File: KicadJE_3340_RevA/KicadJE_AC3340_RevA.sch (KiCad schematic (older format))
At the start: 132 parts

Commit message: Annotate
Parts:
- gave numbers to parts that had none: 125

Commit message: Update KicadJE_AC3340_RevA.sch
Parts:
- removed D119: LED, LED_SMD:LED_0805_2012Metric_Pad1.15x1.40mm_HandSolder, symbol Device:LED
- added R?: OPEN, Resistor_SMD:R_0805_2012Metric_Pad1.15x1.40mm_HandSolder, symbol Device:R
- R156: value 1k -> 100k
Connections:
- net 3CVIn1: now also R156.1
- net 3Octave: now also R151.2, U103.3 (+)
- net GND: now also R?.2
- net at R150.2, R153.2, U103.7: no longer R151.2, U103.3 (+)
- net at R152.2, U103.2 (-): now also R?.1
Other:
- moved on the sheet: R151, R152, R156, U103A
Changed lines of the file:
@@
 L Amplifier_Operational:TL072 U?
 U 1 1 614891B3
-P 7725 4275
+P 9750 6075
 AR Path="/5D99B81E/614891B3" Ref="U?"  Part="3"
 AR Path="/5D99B7BA/614891B3" Ref="U?"  Part="1"
@@
 AR Path="/5F49A670/614891B3" Ref="U?"  Part="1"
 AR Path="/614891B3" Ref="U103"  Part="1"
-F 0 "U103" H 7625 4300 50  0000 C CNN
-F 1 "TL072" H 7650 4225 50  0000 C CNN
-F 2 "AJ-Dropbox-Kicad:AJ_SO-8_5.3x6.2mm_P1.27mm" H 7725 4275 50  0001 C CNN
-F 3 "http://www.ti.com/lit/ds/symlink/tl071.pdf" H 7725 4275 50  0001 C CNN
-	1    7725 4275
+F 0 "U103" H 9650 6100 50  0000 C CNN
+F 1 "TL072" H 9675 6025 50  0000 C CNN
+F 2 "AJ-Dropbox-Kicad:AJ_SO-8_5.3x6.2mm_P1.27mm" H 9750 6075 50  0001 C CNN
+F 3 "http://www.ti.com/lit/ds/symlink/tl071.pdf" H 9750 6075 50  0001 C CNN
+	1    9750 6075
 	1    0    0    -1
 $EndComp
 Wire Wire Line
-	7425 4375 7400 4375
+	9450 6175 9425 6175
 Wire Wire Line
-	7400 4375 7400 4525
+	9425 6175 9425 6325
 Wire Wire Line
-	7400 4525 7575 4525
+	9425 6325 9600 6325
 Wire Wire Line
-	8050 4525 8050 4275
+	10075 6325 10075 6075
 Wire Wire Line
-	8050 4275 8025 4275
+	10075 6075 10050 6075
 $Comp
 L Device:R R156
 U 1 1 614891BF
-P 8200 4275
+P 10225 6075
 AR Path="/614891BF" Ref="R156"  Part="1"
 AR Path="/5C8C5FC0/614891BF" Ref="R?"  Part="1"
@@
 AR Path="/5E62ACA1/614891BF" Ref="R?"  Part="1"
 AR Path="/5F49A670/614891BF" Ref="R?"  Part="1"
-F 0 "R156" V 8100 4200 50  0000 C CNN
-F 1 "1k" V 8200 4275 50  0000 C CNN
-F 2 "Resistor_SMD:R_0805_2012Metric_Pad1.15x1.40mm_HandSolder" V 8130 4275 50  0001 C CNN
-F 3 "~" H 8200 4275 50  0001 C CNN
-	1    8200 4275
+F 0 "R156" V 10125 6000 50  0000 C CNN
+F 1 "100k" V 10225 6075 50  0000 C CNN
+F 2 "Resistor_SMD:R_0805_2012Metric_Pad1.15x1.40mm_HandSolder" V 10155 6075 50  0001 C CNN
+F 3 "~" H 10225 6075 50  0001 C CNN
+	1    10225 6075
 	0    1    1    0
 $EndComp
-Connection ~ 8050 4275
+Connection ~ 10075 6075
 Wire Wire Line
 	2400 1125 2325 1125
@@
 L Device:R R151
 U 1 1 61551447
-P 7725 3950
+P 9750 5750
 AR Path="/61551447" Ref="R151"  Part="1"
 AR Path="/5C8C5FC0/61551447" Ref="R?"  Part="1"
@@
 AR Path="/5E62ACA1/61551447" Ref="R?"  Part="1"
 AR Path="/5F49A670/61551447" Ref="R?"  Part="1"
-F 0 "R151" V 7625 3875 50  0000 C CNN
-F 1 "OPEN" V 7725 3950 50  0000 C CNN
-F 2 "Resistor_SMD:R_0805_2012Metric_Pad1.15x1.40mm_HandSolder" V 7655 3950 50  0001 C CNN
-F 3 "~" H 7725 3950 50  0001 C CNN
-	1    7725 3950
+F 0 "R151" V 9650 5675 50  0000 C CNN
+F 1 "OPEN" V 9750 5750 50  0000 C CNN
+F 2 "Resistor_SMD:R_0805_2012Metric_Pad1.15x1.40mm_HandSolder" V 9680 5750 50  0001 C CNN
+F 3 "~" H 9750 5750 50  0001 C CNN
+	1    9750 5750
 	0    1    1    0
 $EndComp
 Wire Wire Line
-	7400 4175 7400 3950
+	9425 5975 9425 5750
 Wire Wire Line
-	7400 3950 7575 3950
+	9425 5750 9600 5750
 Wire Wire Line
-	7400 4175 7425 4175
+	9425 5975 9450 5975
 Wire Wire Line
-	8050 4275 8050 3950
+	10075 6075 10075 5750
 Wire Wire Line
-	8050 3950 7875 3950
+	10075 5750 9900 5750
 $Comp
 L Envelope-cache-2018-08-04-13-00-04:GND #PWR0125
@@
 Wire Wire Line
 	7550 3750 7400 3750
-Wire Wire Line
-	7400 3750 7400 3950
-Connection ~ 7400 3950
 $Comp
 L Device:R R152
 U 1 1 616AB5FE
-P 7725 4525
+P 9750 6325
 AR Path="/616AB5FE" Ref="R152"  Part="1"
 AR Path="/5C8C5FC0/616AB5FE" Ref="R?"  Part="1"
@@
 AR Path="/5E62ACA1/616AB5FE" Ref="R?"  Part="1"
 AR Path="/5F49A670/616AB5FE" Ref="R?"  Part="1"
-F 0 "R152" V 7825 4450 50  0000 C CNN
-F 1 "0R" V 7725 4525 50  0000 C CNN
-F 2 "Resistor_SMD:R_0805_2012Metric_Pad1.15x1.40mm_HandSolder" V 7655 4525 50  0001 C CNN
-F 3 "~" H 7725 4525 50  0001 C CNN
-	1    7725 4525
+F 0 "R152" V 9850 6250 50  0000 C CNN
+F 1 "0R" V 9750 6325 50  0000 C CNN
+F 2 "Resistor_SMD:R_0805_2012Metric_Pad1.15x1.40mm_HandSolder" V 9680 6325 50  0001 C CNN
+F 3 "~" H 9750 6325 50  0001 C CNN
+	1    9750 6325
 	0    1    1    0
 $EndComp
 Wire Wire Line
-	7875 4525 8050 4525
+	9900 6325 10075 6325
+Text GLabel 10525 6075 2    50   Input ~ 0
+3CVIn1
+Wire Wire Line
+	10375 6075 10525 6075
+Text GLabel 9300 5975 0    50   Input ~ 0
+3Octave
+Wire Wire Line
+	9300 5975 9425 5975
+Connection ~ 9425 5975
 $Comp
-L Device:LED D?
-U 1 1 616ABD5F
-P 8375 4500
-AR Path="/5E4B0DD9/616ABD5F" Ref="D?"  Part="1"
-AR Path="/5E62ACA1/616ABD5F" Ref="D?"  Part="1"
-AR Path="/5F49A670/616ABD5F" Ref="D?"  Part="1"
-AR Path="/616ABD5F" Ref="D119"  Part="1"
-F 0 "D119" H 8525 4575 50  0000 R CNN
-F 1 "LED" H 8475 4650 50  0000 R CNN
-F 2 "LED_SMD:LED_0805_2012Metric_Pad1.15x1.40mm_HandSolder" H 8375 4500 50  0001 C CNN
-F 3 "~" H 8375 4500 50  0001 C CNN
-	1    8375 4500
-	0    -1   -1   0
+L Device:R R?
+U 1 1 5E78950E
+P 9200 6325
+AR Path="/5E78950E" Ref="R?"  Part="1"
+AR Path="/5C8C5FC0/5E78950E" Ref="R?"  Part="1"
+AR Path="/5CAAE8D3/5E78950E" Ref="R?"  Part="1"
+AR Path="/5E4B0DD9/5E78950E" Ref="R?"  Part="1"
+AR Path="/5E62ACA1/5E78950E" Ref="R?"  Part="1"
+AR Path="/5F49A670/5E78950E" Ref="R?"  Part="1"
+F 0 "R?" V 9100 6250 50  0000 C CNN
+F 1 "OPEN" V 9200 6325 50  0000 C CNN
+F 2 "Resistor_SMD:R_0805_2012Metric_Pad1.15x1.40mm_HandSolder" V 9130 6325 50  0001 C CNN
+F 3 "~" H 9200 6325 50  0001 C CNN
+	1    9200 6325
+	0    1    1    0
 $EndComp
 $Comp
-L Envelope-cache-2018-08-04-13-00-04:GND #PWR0142
-U 1 1 616AD7D0
-P 8375 4700
-AR Path="/616AD7D0" Ref="#PWR0142"  Part="1"
-AR Path="/5C8C5FC0/616AD7D0" Ref="#PWR?"  Part="1"
-AR Path="/5CAAE8D3/616AD7D0" Ref="#PWR?"  Part="1"
-AR Path="/5E4B0DD9/616AD7D0" Ref="#PWR?"  Part="1"
-AR Path="/5E62ACA1/616AD7D0" Ref="#PWR?"  Part="1"
-AR Path="/5F49A670/616AD7D0" Ref="#PWR?"  Part="1"
-F 0 "#PWR0142" H 8375 4450 50  0001 C CNN
-F 1 "GND" H 8380 4527 50  0000 C CNN
-F 2 "" H 8375 4700 50  0001 C CNN
-F 3 "" H 8375 4700 50  0001 C CNN
-	1    8375 4700
+L Envelope-cache-2018-08-04-13-00-04:GND #PWR?
+U 1 1 5E789A07
+P 8975 6325
+AR Path="/5E789A07" Ref="#PWR?"  Part="1"
+AR Path="/5C8C5FC0/5E789A07" Ref="#PWR?"  Part="1"
+AR Path="/5CAAE8D3/5E789A07" Ref="#PWR?"  Part="1"
+AR Path="/5E4B0DD9/5E789A07" Ref="#PWR?"  Part="1"
+AR Path="/5E62ACA1/5E789A07" Ref="#PWR?"  Part="1"
+AR Path="/5F49A670/5E789A07" Ref="#PWR?"  Part="1"
+F 0 "#PWR?" H 8975 6075 50  0001 C CNN
+F 1 "GND" H 8980 6152 50  0000 C CNN
+F 2 "" H 8975 6325 50  0001 C CNN
+F 3 "" H 8975 6325 50  0001 C CNN
+	1    8975 6325
 	1    0    0    -1
 $EndComp
 Wire Wire Line
-	8375 4700 8375 4650
+	8975 6325 9050 6325
 Wire Wire Line
-	8375 4275 8350 4275
-Wire Wire Line
-	8375 4350 8375 4275
+	9350 6325 9425 6325
+Connection ~ 9425 6325
 $EndSCHEMATC

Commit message: base PCB
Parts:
- gave numbers to parts that had none: 1
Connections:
- net +12L is gone; now on net +12VA: R117.2
- net +12V is gone; now on net +12VA: D101.1 (K), D103.1 (K), D105.1 (K), D106.1 (K), D109.1 (K), D111.1 (K), R129.1
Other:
- moved on the sheet: J111, R151, R152, R156, R163, U103A

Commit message: DRC Done
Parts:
- added C118, C119: 100n, Capacitor_SMD:C_0805_2012Metric_Pad1.15x1.40mm_HandSolder, symbol Device:C
- added unit 3 of U103
- added unit 3 of U107
- D115: footprint (none) -> Diode_THT:D_A-405_P7.62mm_Horizontal
- Q102: footprint UMT6 -> AJ:UMX1N_UMT6_DualNPN
- U104: footprint (none) -> Package_DIP:DIP-16_W10.16mm_LongPads
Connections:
- net +12VA: now also C118.1, U103.8 (V+), U107.8 (V+)
- net -12VA: now also C119.2, U103.4 (V-), U107.4 (V-)
- net GND: now also C118.2, C119.1
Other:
- moved on the sheet: C112, C113, C114, C115, C116, C117, D117, D118, U102C, U105, U106

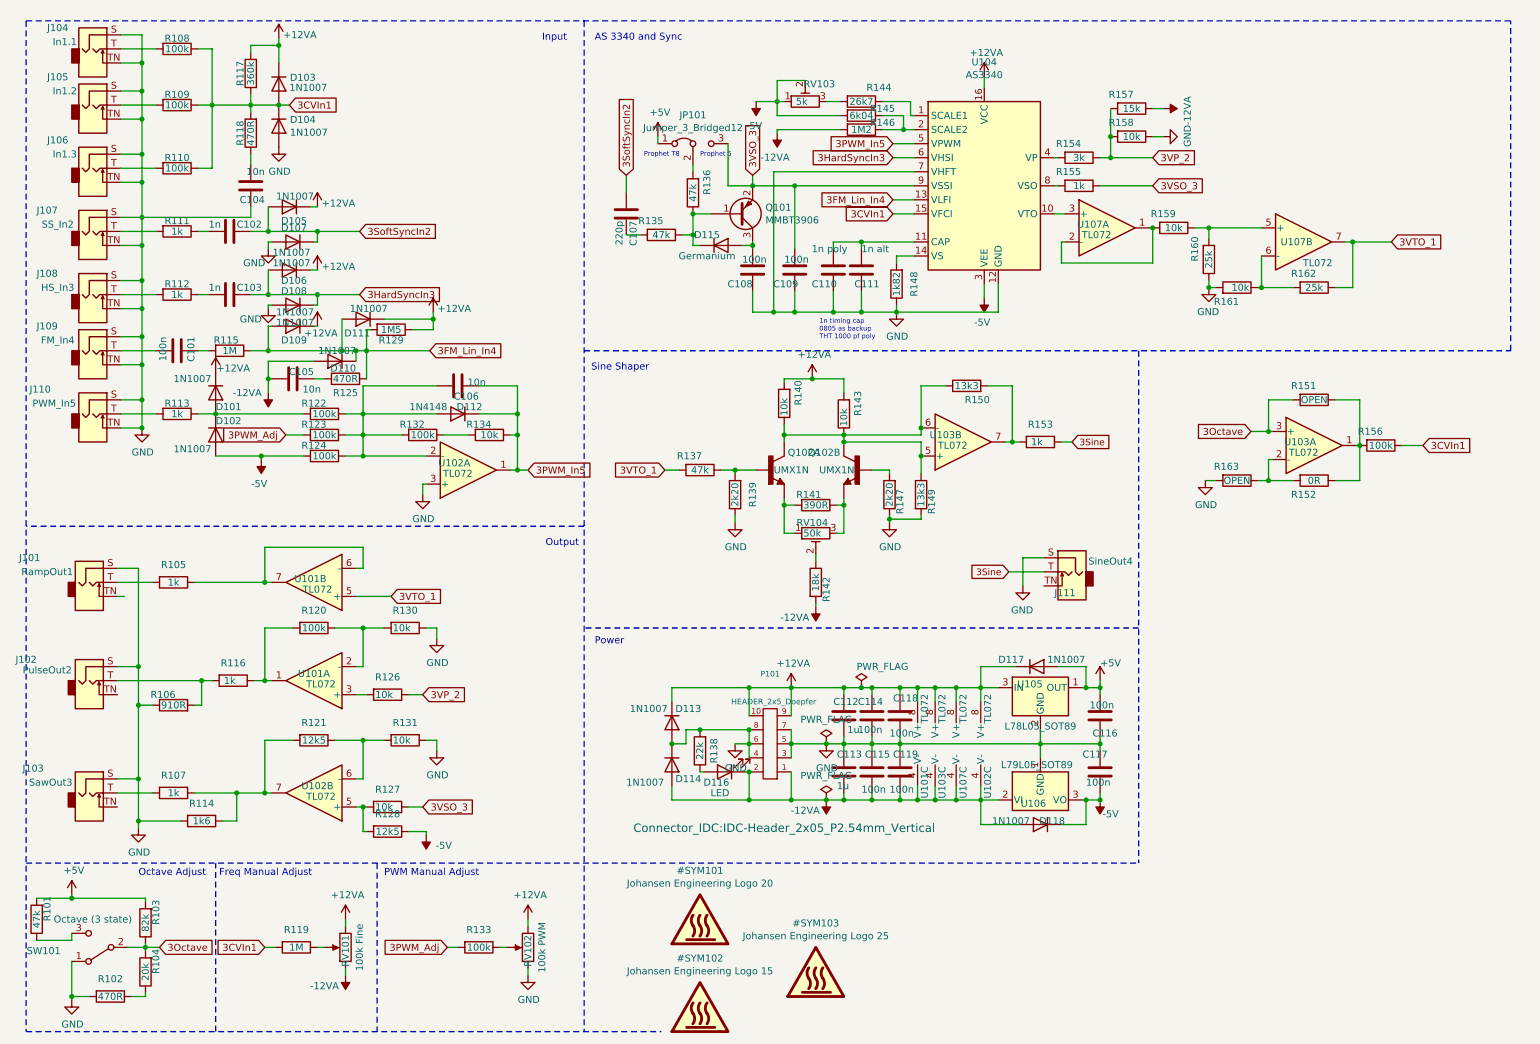
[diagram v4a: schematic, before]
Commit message: Minor rearrangement
remove 2 labels
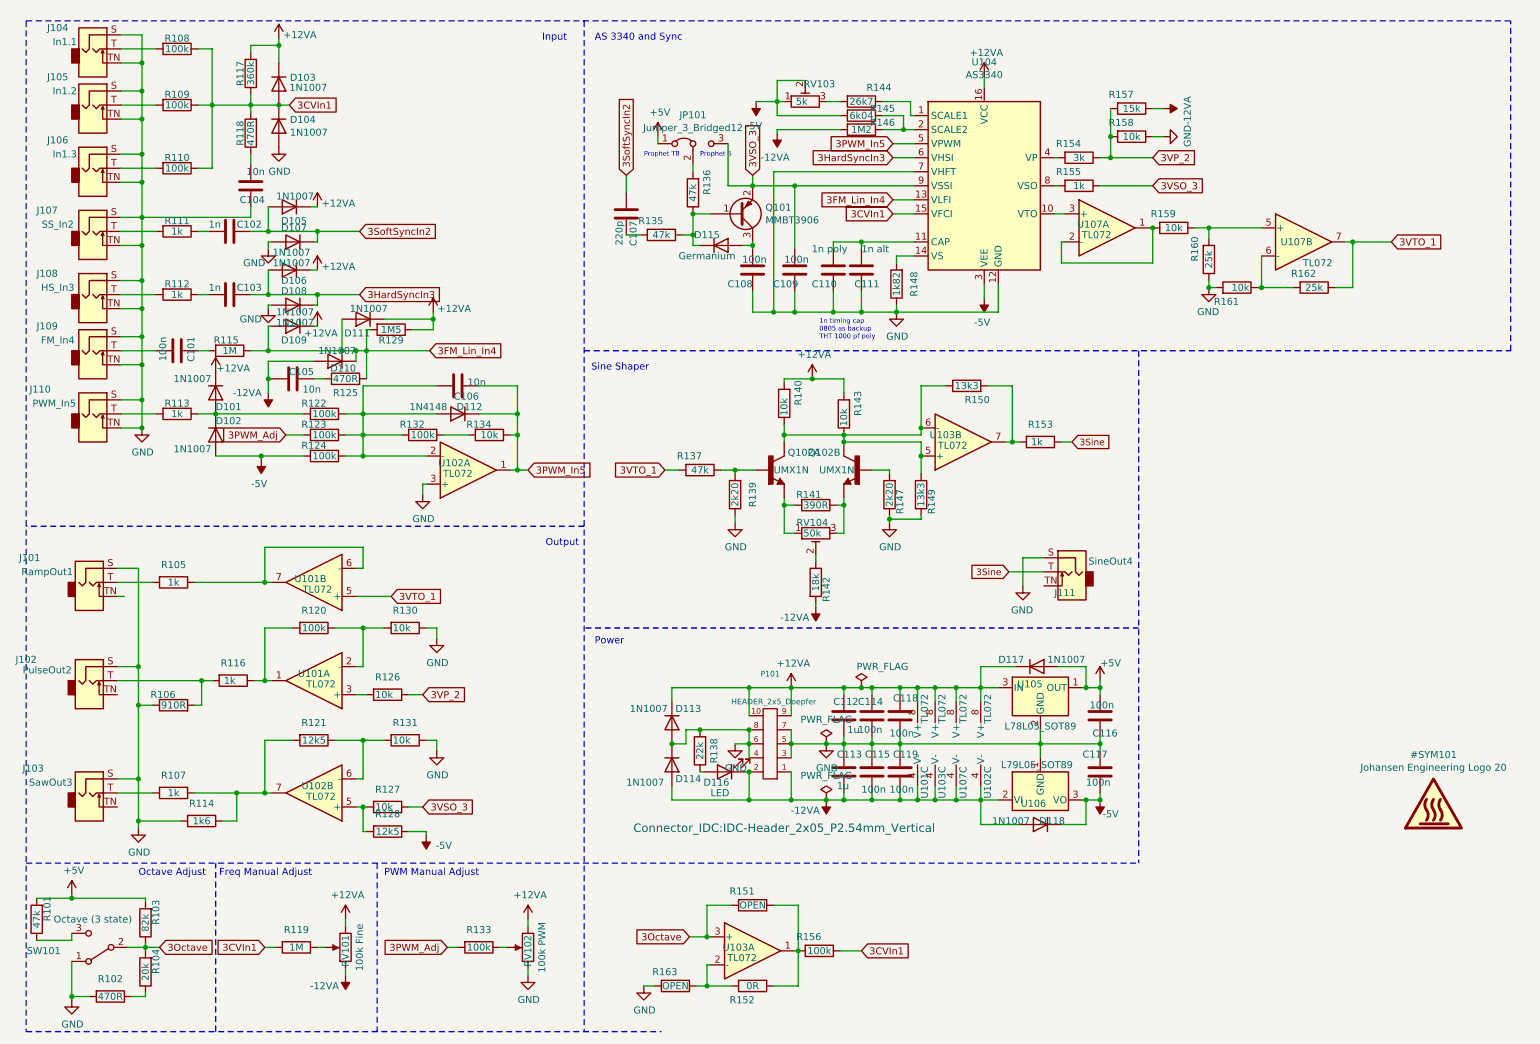
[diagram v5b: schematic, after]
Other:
- moved on the sheet: R151, R152, R156, R163, U103A
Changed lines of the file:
@@
 $Comp
 L Graphic:SYM_Hot_Large #SYM?
-U 1 1 5F4B935E
-P 5325 7525
-AR Path="/5E4B0DD9/5F4B935E" Ref="#SYM?"  Part="1"
-AR Path="/5F49A670/5F4B935E" Ref="#SYM?"  Part="1"
-AR Path="/5F4B935E" Ref="#SYM102"  Part="1"
-F 0 "#SYM102" H 5325 7847 50  0000 C CNN
-F 1 "Johansen Engineering Logo 15" H 5325 7756 50  0000 C CNN
-F 2 "AJ:Johansen_engineering_logo_15mm" H 5325 7325 50  0001 C CNN
-F 3 "~" H 5355 7325 50  0001 C CNN
-	1    5325 7525
-	1    0    0    -1
-$EndComp
-$Comp
-L Graphic:SYM_Hot_Large #SYM?
 U 1 1 5F4B9364
-P 5325 6900
+P 10550 6075
 AR Path="/5E4B0DD9/5F4B9364" Ref="#SYM?"  Part="1"
 AR Path="/5F49A670/5F4B9364" Ref="#SYM?"  Part="1"
 AR Path="/5F4B9364" Ref="#SYM101"  Part="1"
-F 0 "#SYM101" H 5325 7222 50  0000 C CNN
-F 1 "Johansen Engineering Logo 20" H 5325 7131 50  0000 C CNN
-F 2 "AJ:Johansen_engineering_logo_20mm" H 5325 6700 50  0001 C CNN
-F 3 "~" H 5355 6700 50  0001 C CNN
-	1    5325 6900
-	1    0    0    -1
-$EndComp
-$Comp
-L Graphic:SYM_Hot_Large #SYM?
-U 1 1 5F4B936A
-P 6150 7275
-AR Path="/5E4B0DD9/5F4B936A" Ref="#SYM?"  Part="1"
-AR Path="/5F49A670/5F4B936A" Ref="#SYM?"  Part="1"
-AR Path="/5F4B936A" Ref="#SYM103"  Part="1"
-F 0 "#SYM103" H 6150 7597 50  0000 C CNN
-F 1 "Johansen Engineering Logo 25" H 6150 7506 50  0000 C CNN
-F 2 "AJ:Johansen_engineering_logo_25mm_front_neg5" H 6150 7075 50  0001 C CNN
-F 3 "~" H 6180 7075 50  0001 C CNN
-	1    6150 7275
+F 0 "#SYM101" H 10550 6397 50  0000 C CNN
+F 1 "Johansen Engineering Logo 20" H 10550 6306 50  0000 C CNN
+F 2 "AJ:Johansen_engineering_logo_20mm" H 10550 5875 50  0001 C CNN
+F 3 "~" H 10580 5875 50  0001 C CNN
+	1    10550 6075
 	1    0    0    -1
 $EndComp
@@
 L Amplifier_Operational:TL072 U?
 U 1 1 614891B3
-P 9700 3550
+P 5700 7150
 AR Path="/5D99B81E/614891B3" Ref="U?"  Part="3"
 AR Path="/5D99B7BA/614891B3" Ref="U?"  Part="1"
@@
 AR Path="/5F49A670/614891B3" Ref="U?"  Part="1"
 AR Path="/614891B3" Ref="U103"  Part="1"
-F 0 "U103" H 9600 3575 50  0000 C CNN
-F 1 "TL072" H 9625 3500 50  0000 C CNN
-F 2 "AJ-Dropbox-Kicad:AJ_SO-8_5.3x6.2mm_P1.27mm" H 9700 3550 50  0001 C CNN
-F 3 "http://www.ti.com/lit/ds/symlink/tl071.pdf" H 9700 3550 50  0001 C CNN
-	1    9700 3550
+F 0 "U103" H 5600 7175 50  0000 C CNN
+F 1 "TL072" H 5625 7100 50  0000 C CNN
+F 2 "AJ-Dropbox-Kicad:AJ_SO-8_5.3x6.2mm_P1.27mm" H 5700 7150 50  0001 C CNN
+F 3 "http://www.ti.com/lit/ds/symlink/tl071.pdf" H 5700 7150 50  0001 C CNN
+	1    5700 7150
 	1    0    0    -1
 $EndComp
 Wire Wire Line
-	9400 3650 9375 3650
+	5400 7250 5375 7250
 Wire Wire Line
-	9375 3650 9375 3800
+	5375 7250 5375 7400
 Wire Wire Line
-	9375 3800 9550 3800
+	5375 7400 5550 7400
 Wire Wire Line
-	10025 3800 10025 3550
+	6025 7400 6025 7150
 Wire Wire Line
-	10025 3550 10000 3550
+	6025 7150 6000 7150
 $Comp
 L Device:R R156
 U 1 1 614891BF
-P 10175 3550
+P 6175 7150
 AR Path="/614891BF" Ref="R156"  Part="1"
 AR Path="/5C8C5FC0/614891BF" Ref="R?"  Part="1"
@@
 AR Path="/5E62ACA1/614891BF" Ref="R?"  Part="1"
 AR Path="/5F49A670/614891BF" Ref="R?"  Part="1"
-F 0 "R156" V 10075 3475 50  0000 C CNN
-F 1 "100k" V 10175 3550 50  0000 C CNN
-F 2 "Resistor_SMD:R_0805_2012Metric_Pad1.15x1.40mm_HandSolder" V 10105 3550 50  0001 C CNN
-F 3 "~" H 10175 3550 50  0001 C CNN
-	1    10175 3550
+F 0 "R156" V 6075 7075 50  0000 C CNN
+F 1 "100k" V 6175 7150 50  0000 C CNN
+F 2 "Resistor_SMD:R_0805_2012Metric_Pad1.15x1.40mm_HandSolder" V 6105 7150 50  0001 C CNN
+F 3 "~" H 6175 7150 50  0001 C CNN
+	1    6175 7150
 	0    1    1    0
 $EndComp
-Connection ~ 10025 3550
+Connection ~ 6025 7150
 Wire Wire Line
 	2400 1125 2325 1125
@@
 L Device:R R151
 U 1 1 61551447
-P 9700 3225
+P 5700 6825
 AR Path="/61551447" Ref="R151"  Part="1"
 AR Path="/5C8C5FC0/61551447" Ref="R?"  Part="1"
@@
 AR Path="/5E62ACA1/61551447" Ref="R?"  Part="1"
 AR Path="/5F49A670/61551447" Ref="R?"  Part="1"
-F 0 "R151" V 9600 3150 50  0000 C CNN
-F 1 "OPEN" V 9700 3225 50  0000 C CNN
-F 2 "Resistor_SMD:R_0805_2012Metric_Pad1.15x1.40mm_HandSolder" V 9630 3225 50  0001 C CNN
-F 3 "~" H 9700 3225 50  0001 C CNN
-	1    9700 3225
+F 0 "R151" V 5600 6750 50  0000 C CNN
+F 1 "OPEN" V 5700 6825 50  0000 C CNN
+F 2 "Resistor_SMD:R_0805_2012Metric_Pad1.15x1.40mm_HandSolder" V 5630 6825 50  0001 C CNN
+F 3 "~" H 5700 6825 50  0001 C CNN
+	1    5700 6825
 	0    1    1    0
 $EndComp
 Wire Wire Line
-	9375 3450 9375 3225
+	5375 7050 5375 6825
 Wire Wire Line
-	9375 3225 9550 3225
+	5375 6825 5550 6825
 Wire Wire Line
-	9375 3450 9400 3450
+	5375 7050 5400 7050
 Wire Wire Line
-	10025 3550 10025 3225
+	6025 7150 6025 6825
 Wire Wire Line
-	10025 3225 9850 3225
+	6025 6825 5850 6825
 $Comp
 L Envelope-cache-2018-08-04-13-00-04:GND #PWR0125
@@
 L Device:R R152
 U 1 1 616AB5FE
-P 9700 3800
+P 5700 7400
 AR Path="/616AB5FE" Ref="R152"  Part="1"
 AR Path="/5C8C5FC0/616AB5FE" Ref="R?"  Part="1"
@@
 AR Path="/5E62ACA1/616AB5FE" Ref="R?"  Part="1"
 AR Path="/5F49A670/616AB5FE" Ref="R?"  Part="1"
-F 0 "R152" V 9800 3725 50  0000 C CNN
-F 1 "0R" V 9700 3800 50  0000 C CNN
-F 2 "Resistor_SMD:R_0805_2012Metric_Pad1.15x1.40mm_HandSolder" V 9630 3800 50  0001 C CNN
-F 3 "~" H 9700 3800 50  0001 C CNN
-	1    9700 3800
+F 0 "R152" V 5800 7325 50  0000 C CNN
+F 1 "0R" V 5700 7400 50  0000 C CNN
+F 2 "Resistor_SMD:R_0805_2012Metric_Pad1.15x1.40mm_HandSolder" V 5630 7400 50  0001 C CNN
+F 3 "~" H 5700 7400 50  0001 C CNN
+	1    5700 7400
 	0    1    1    0
 $EndComp
 Wire Wire Line
-	9850 3800 10025 3800
-Text GLabel 10475 3550 2    50   Input ~ 0
+	5850 7400 6025 7400
+Text GLabel 6475 7150 2    50   Input ~ 0
 3CVIn1
 Wire Wire Line
-	10325 3550 10475 3550
-Text GLabel 9250 3450 0    50   Input ~ 0
+	6325 7150 6475 7150
+Text GLabel 5250 7050 0    50   Input ~ 0
 3Octave
 Wire Wire Line
-	9250 3450 9375 3450
-Connection ~ 9375 3450
+	5250 7050 5375 7050
+Connection ~ 5375 7050
 $Comp
 L Device:R R163
 U 1 1 5E78950E
-P 9150 3800
+P 5150 7400
 AR Path="/5E78950E" Ref="R163"  Part="1"
 AR Path="/5C8C5FC0/5E78950E" Ref="R?"  Part="1"
@@
 AR Path="/5E62ACA1/5E78950E" Ref="R?"  Part="1"
 AR Path="/5F49A670/5E78950E" Ref="R?"  Part="1"
-F 0 "R163" V 9050 3725 50  0000 C CNN
-F 1 "OPEN" V 9150 3800 50  0000 C CNN
-F 2 "Resistor_SMD:R_0805_2012Metric_Pad1.15x1.40mm_HandSolder" V 9080 3800 50  0001 C CNN
-F 3 "~" H 9150 3800 50  0001 C CNN
-	1    9150 3800
+F 0 "R163" V 5050 7325 50  0000 C CNN
+F 1 "OPEN" V 5150 7400 50  0000 C CNN
+F 2 "Resistor_SMD:R_0805_2012Metric_Pad1.15x1.40mm_HandSolder" V 5080 7400 50  0001 C CNN
+F 3 "~" H 5150 7400 50  0001 C CNN
+	1    5150 7400
 	0    1    1    0
 $EndComp
@@
 L Envelope-cache-2018-08-04-13-00-04:GND #PWR0142
 U 1 1 5E789A07
-P 8925 3800
+P 4925 7400
 AR Path="/5E789A07" Ref="#PWR0142"  Part="1"
 AR Path="/5C8C5FC0/5E789A07" Ref="#PWR?"  Part="1"
@@
 AR Path="/5E62ACA1/5E789A07" Ref="#PWR?"  Part="1"
 AR Path="/5F49A670/5E789A07" Ref="#PWR?"  Part="1"
-F 0 "#PWR0142" H 8925 3550 50  0001 C CNN
-F 1 "GND" H 8930 3627 50  0000 C CNN
-F 2 "" H 8925 3800 50  0001 C CNN
-F 3 "" H 8925 3800 50  0001 C CNN
-	1    8925 3800
+F 0 "#PWR0142" H 4925 7150 50  0001 C CNN
+F 1 "GND" H 4930 7227 50  0000 C CNN
+F 2 "" H 4925 7400 50  0001 C CNN
+F 3 "" H 4925 7400 50  0001 C CNN
+	1    4925 7400
 	1    0    0    -1
 $EndComp
 Wire Wire Line
-	8925 3800 9000 3800
+	4925 7400 5000 7400
 Wire Wire Line
-	9300 3800 9375 3800
-Connection ~ 9375 3800
+	5300 7400 5375 7400
+Connection ~ 5375 7400
 Wire Wire Line
 	2325 825  2325 700
